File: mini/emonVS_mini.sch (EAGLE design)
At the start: 17 parts, among them J7 RJ45 Jack, J8 TERMINAL_BLOCK_2P, M1 275VAC, T1 ZMPT101B

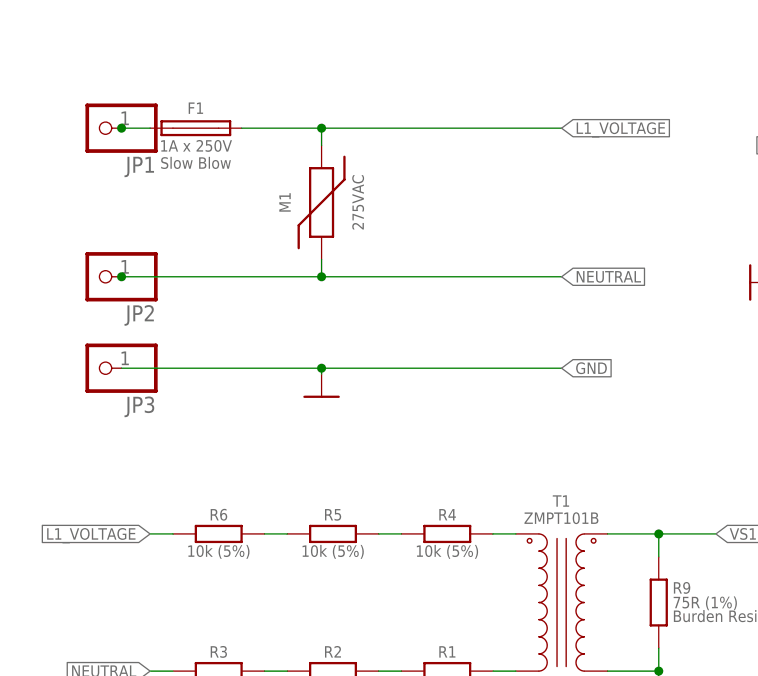
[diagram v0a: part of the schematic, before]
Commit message: improved thermal, swap around earth neutral, 0R link option
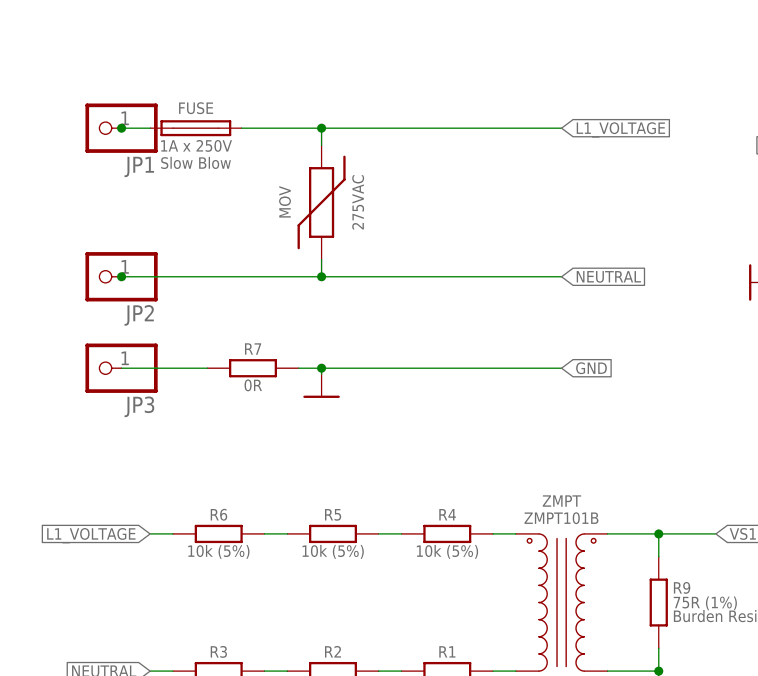
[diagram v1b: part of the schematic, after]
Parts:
- added R7: 0R, My-RLC:R_1206
- renumbered F1 to FUSE, M1 to MOV, T1 to ZMPT
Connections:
- new net N$8: JP3.1, R7.2
- net GND: now also R7.1; no longer JP3.1
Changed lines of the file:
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@@
 <setting verticaltext="up"/>
 </settings>
-<grid distance="0.1" unitdist="inch" unit="inch" style="lines" multiple="1" display="no" altdistance="0.01" altunitdist="inch" altunit="inch"/>
+<grid distance="0.025" unitdist="inch" unit="inch" style="lines" multiple="1" display="no" altdistance="0.01" altunitdist="inch" altunit="inch"/>
 <layers>
 <layer number="1" name="Top" color="59" fill="1" visible="no" active="no"/>
@@
 </groups>
 <parts>
-<part name="T1" library="OpenEnergyMonitor" deviceset="ZMPT101B" device=""/>
+<part name="ZMPT" library="OpenEnergyMonitor" deviceset="ZMPT101B" device=""/>
 <part name="R1" library="My-RLC" library_urn="urn:adsk.eagle:library:35509816" deviceset="R_" device="1206" package3d_urn="urn:adsk.eagle:package:35509967/1" value="10k (5%)">
 <attribute name="PN" value="ERJ-H3GJ103V"/>
@@
 <attribute name="PN" value="ERJ-H3GJ103V"/>
 </part>
-<part name="F1" library="OpenEnergyMonitor" deviceset="FUSE" device="" value="1A x 250V"/>
-<part name="M1" library="OpenEnergyMonitor" deviceset="MOV_" device="14MM_275VAC" value="275VAC"/>
+<part name="FUSE" library="OpenEnergyMonitor" deviceset="FUSE" device="" value="1A x 250V"/>
+<part name="MOV" library="OpenEnergyMonitor" deviceset="MOV_" device="14MM_275VAC" value="275VAC"/>
 <part name="FD1" library="OpenEnergyMonitor" deviceset="FIDUCIAL" device="1X2"/>
 <part name="FD2" library="OpenEnergyMonitor" deviceset="FIDUCIAL" device="1X2"/>
@@
 <part name="JP2" library="adafruit" library_urn="urn:adsk.eagle:library:420" deviceset="PINHD-1X1" device="" package3d_urn="urn:adsk.eagle:package:6240654/1"/>
 <part name="JP3" library="adafruit" library_urn="urn:adsk.eagle:library:420" deviceset="PINHD-1X1" device="" package3d_urn="urn:adsk.eagle:package:6240654/1"/>
+<part name="R7" library="My-RLC" library_urn="urn:adsk.eagle:library:35509816" deviceset="R_" device="1206" package3d_urn="urn:adsk.eagle:package:35509967/1" value="0R">
+<attribute name="PN" value="ERJ-H3GJ103V"/>
+</part>
 </parts>
 <sheets>
@@
 </plain>
 <instances>
-<instance part="T1" gate="G$1" x="95.885" y="68.58" smashed="yes" grouprefs="VOLTAGE_MEASUREMENT_PHASE_1">
+<instance part="ZMPT" gate="G$1" x="95.885" y="68.58" smashed="yes" grouprefs="VOLTAGE_MEASUREMENT_PHASE_1">
 <attribute name="NAME" x="95.885" y="79.8576" size="1.27" layer="95" rot="R180" align="center"/>
 <attribute name="VALUE" x="95.885" y="77.9526" size="1.27" layer="96" rot="R180" align="center"/>
@@
 <attribute name="VALUE" x="57.785" y="74.295" size="1.27" layer="96" rot="MR0" align="center"/>
 </instance>
-<instance part="F1" gate="G$1" x="55.245" y="121.285" smashed="yes" rot="R180" grouprefs="SINGLE-PHASE_AC_NETWORK_INTERFACE">
+<instance part="FUSE" gate="G$1" x="55.245" y="121.285" smashed="yes" rot="R180" grouprefs="SINGLE-PHASE_AC_NETWORK_INTERFACE">
 <attribute name="NAME" x="55.245" y="123.5075" size="1.27" layer="95" rot="R180" align="center"/>
 <attribute name="FAMILY" x="55.245" y="117.4115" size="1.27" layer="96" rot="R180" align="center"/>
 <attribute name="VALUE" x="55.245" y="119.3165" size="1.27" layer="96" rot="R180" align="center"/>
 </instance>
-<instance part="M1" gate="G$1" x="69.215" y="113.03" smashed="yes" rot="MR0" grouprefs="SINGLE-PHASE_AC_NETWORK_INTERFACE">
+<instance part="MOV" gate="G$1" x="69.215" y="113.03" smashed="yes" rot="MR0" grouprefs="SINGLE-PHASE_AC_NETWORK_INTERFACE">
 <attribute name="NAME" x="65.151" y="113.03" size="1.27" layer="95" rot="MR90" align="center"/>
 <attribute name="VALUE" x="73.279" y="113.03" size="1.27" layer="96" rot="MR90" align="center"/>
@@
 <attribute name="VALUE" x="50.8" y="99.695" size="1.778" layer="96" rot="R180"/>
 </instance>
+<instance part="R7" gate="G$1" x="61.595" y="94.615" smashed="yes" rot="MR0">
+<attribute name="PN" x="61.595" y="94.615" size="1.778" layer="96" display="off"/>
+<attribute name="NAME" x="61.595" y="96.7486" size="1.27" layer="95" rot="MR0" align="center"/>
+<attribute name="VALUE" x="61.595" y="92.71" size="1.27" layer="96" rot="MR0" align="center"/>
+</instance>
 </instances>
 <busses>
@@
 <wire x1="100.965" y1="76.2" x2="106.68" y2="76.2" width="0.1524" layer="91" grouprefs="VOLTAGE_MEASUREMENT_PHASE_1"/>
 <label x="113.03" y="76.2" size="1.27" layer="95" rot="MR180" xref="yes" grouprefs="VOLTAGE_MEASUREMENT_PHASE_1"/>
-<pinref part="T1" gate="G$1" pin="SEC_2"/>
+<pinref part="ZMPT" gate="G$1" pin="SEC_2"/>
 <pinref part="R9" gate="G$1" pin="1"/>
 <wire x1="106.68" y1="76.2" x2="113.03" y2="76.2" width="0.1524" layer="91" grouprefs="VOLTAGE_MEASUREMENT_PHASE_1"/>
@@
 <wire x1="95.885" y1="104.775" x2="69.215" y2="104.775" width="0.1524" layer="91" grouprefs="SINGLE-PHASE_AC_NETWORK_INTERFACE"/>
 <wire x1="69.215" y1="104.775" x2="46.99" y2="104.775" width="0.1524" layer="91" grouprefs="SINGLE-PHASE_AC_NETWORK_INTERFACE"/>
-<pinref part="M1" gate="G$1" pin="1"/>
+<pinref part="MOV" gate="G$1" pin="1"/>
 <wire x1="69.215" y1="106.68" x2="69.215" y2="104.775" width="0.1524" layer="91" grouprefs="SINGLE-PHASE_AC_NETWORK_INTERFACE"/>
 <junction x="69.215" y="104.775" grouprefs="SINGLE-PHASE_AC_NETWORK_INTERFACE"/>
@@
 <segment>
 <label x="95.885" y="121.285" size="1.27" layer="95" xref="yes" grouprefs="SINGLE-PHASE_AC_NETWORK_INTERFACE"/>
-<pinref part="F1" gate="G$1" pin="1"/>
+<pinref part="FUSE" gate="G$1" pin="1"/>
 <wire x1="60.325" y1="121.285" x2="69.215" y2="121.285" width="0.1524" layer="91" grouprefs="SINGLE-PHASE_AC_NETWORK_INTERFACE"/>
-<pinref part="M1" gate="G$1" pin="2"/>
+<pinref part="MOV" gate="G$1" pin="2"/>
 <wire x1="69.215" y1="119.38" x2="69.215" y2="121.285" width="0.1524" layer="91" grouprefs="SINGLE-PHASE_AC_NETWORK_INTERFACE"/>
 <wire x1="95.885" y1="121.285" x2="69.215" y2="121.285" width="0.1524" layer="91"/>
@@
 <net name="N$7" class="0">
 <segment>
-<pinref part="F1" gate="G$1" pin="2"/>
+<pinref part="FUSE" gate="G$1" pin="2"/>
 <wire x1="46.99" y1="121.285" x2="50.165" y2="121.285" width="0.1524" layer="91" grouprefs="SINGLE-PHASE_AC_NETWORK_INTERFACE"/>
 <pinref part="JP1" gate="G$1" pin="1"/>
@@
 <pinref part="R4" gate="G$1" pin="1"/>
 <wire x1="88.265" y1="76.2" x2="90.805" y2="76.2" width="0.1524" layer="91" grouprefs="VOLTAGE_MEASUREMENT_PHASE_1"/>
-<pinref part="T1" gate="G$1" pin="PRI_1"/>
+<pinref part="ZMPT" gate="G$1" pin="PRI_1"/>
 </segment>
 </net>
@@
 <pinref part="R1" gate="G$1" pin="1"/>
 <wire x1="88.265" y1="60.96" x2="90.805" y2="60.96" width="0.1524" layer="91" grouprefs="VOLTAGE_MEASUREMENT_PHASE_1"/>
-<pinref part="T1" gate="G$1" pin="PRI_2"/>
+<pinref part="ZMPT" gate="G$1" pin="PRI_2"/>
 </segment>
 </net>
 <net name="GND" class="0">
 <segment>
-<pinref part="T1" gate="G$1" pin="SEC_1"/>
+<pinref part="ZMPT" gate="G$1" pin="SEC_1"/>
 <wire x1="100.965" y1="60.96" x2="106.68" y2="60.96" width="0.1524" layer="91" grouprefs="VOLTAGE_MEASUREMENT_PHASE_1"/>
 <pinref part="SUPPLY3" gate="G$1" pin="0V"/>
@@
 </segment>
 <segment>
-<wire x1="46.99" y1="94.615" x2="69.215" y2="94.615" width="0.1524" layer="91" grouprefs="SINGLE-PHASE_AC_NETWORK_INTERFACE"/>
 <label x="95.885" y="94.615" size="1.27" layer="95" xref="yes" grouprefs="SINGLE-PHASE_AC_NETWORK_INTERFACE"/>
 <pinref part="SUPPLY6" gate="G$1" pin="0V"/>
-<wire x1="69.215" y1="94.615" x2="95.885" y2="94.615" width="0.1524" layer="91" grouprefs="SINGLE-PHASE_AC_NETWORK_INTERFACE"/>
 <wire x1="69.215" y1="93.98" x2="69.215" y2="94.615" width="0.1524" layer="91" grouprefs="SINGLE-PHASE_AC_NETWORK_INTERFACE"/>
-<junction x="69.215" y="94.615" grouprefs="SINGLE-PHASE_AC_NETWORK_INTERFACE"/>
-<pinref part="JP3" gate="G$1" pin="1"/>
+<pinref part="R7" gate="G$1" pin="1"/>
+<wire x1="66.675" y1="94.615" x2="69.215" y2="94.615" width="0.1524" layer="91"/>
+<wire x1="69.215" y1="94.615" x2="95.885" y2="94.615" width="0.1524" layer="91"/>
+<junction x="69.215" y="94.615"/>
 </segment>
 <segment>
@@
 </segment>
 </net>
+<net name="N$8" class="0">
+<segment>
+<pinref part="JP3" gate="G$1" pin="1"/>
+<pinref part="R7" gate="G$1" pin="2"/>
+<wire x1="46.99" y1="94.615" x2="56.515" y2="94.615" width="0.1524" layer="91"/>
+</segment>
+</net>
